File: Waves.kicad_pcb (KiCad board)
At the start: 2 copper layers, 49.8 x 106.5 mm, 147 parts, among them J1 AudioJack2_SwitchT, J10 AudioJack2_SwitchT, J11 Conn_01x04_Male, J12 Conn_01x04_Male, J13 AudioJack2_SwitchT, J14 AudioJack2_SwitchT, J15 Conn_02x05_Odd_Even, J2 AudioJack2_SwitchT, J3 AudioJack2_SwitchT, J4 AudioJack2_SwitchT, J5 AudioJack2_SwitchT, J6 AudioJack2_SwitchT, J7 AudioJack2_SwitchT, J8 AudioJack2_SwitchT, J9 AudioJack2_SwitchT, Q1 BC847, Q2 BC847, Q3 BC847, Q4 BC847, Q5 BC847, SW1 SW_Push, SW2 Rotary_Encoder_Switch, SW3 SW_Push_LED, SW4 SW_Push_LED, SW5 SW_Push_LED, U1 STM32G431, U2 AT25xxx, U3 IPS240x240, U4 PCM5100, U5 TL072, U6 LM1117-3.3, U7 LM1117-3.3, U8 MCP6004, U9 MCP6004, Y1 8MHz

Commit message: Placed front-side components.
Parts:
- C1, C10, C11, C12, C13, C14, C15, C16, C17, C18, C19, C2, C20, C21, C22, C23, C24, C25, C26, C27, C28, C29, C3, C30, C31, C32, C33, C34, C35, C36, C37, C38, C39, C4, C40, C41, C42, C43, C44, C45, C46, C47, C48, C49, C5, C50, C51, C52, C6, C7, C8, C9, D1, D2, D3, D4, FB1, FB2, FB3, J11, J12, J15, L1, Q1, Q2, Q3, Q4, Q5, R1, R10, R11, R12, R13, R14, R15, R16, R17, R18, R19, R2, R20, R21, R22, R23, R24, R25, R26, R27, R28, R29, R3, R30, R31, R32, R33, R34, R35, R36, R37, R38, R39, R4, R40, R41, R42, R43, R44, R45, R46, R5, R6, R7, R8, R9, TP1, TP2, TP3, TP4, TP5, TP6, U1, U2, U4, U5, U6, U7, U8, U9, Y1: moved to B.Cu
- moved R19 193.5 mm to (111.3, 147.6)
- moved Q3 192.8 mm to (107.1, 146.6)
- moved R20 191.7 mm to (111.3, 145.1)
- moved R21 165.0 mm to (142.9, 89.7), turned to 90 degrees
- moved Q4 162.4 mm to (146.4, 89.4), turned to 90 degrees
- moved SW4 157.9 mm to (144.6, 96.6)
- moved C25 147.6 mm to (181.0, 163.3)
- moved R6 147.6 mm to (185.0, 163.3)
- moved C21 147.3 mm to (176.8, 163.1)
- moved J9 146.7 mm to (109.1, 147.3)
- moved U5 146.1 mm to (162.3, 162.3)
- moved C20 145.2 mm to (170.7, 161.7)
- moved C22 144.0 mm to (185.0, 160.8)
- moved R10 144.0 mm to (181.0, 160.8)
- moved C28 143.4 mm to (176.6, 160.4)
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
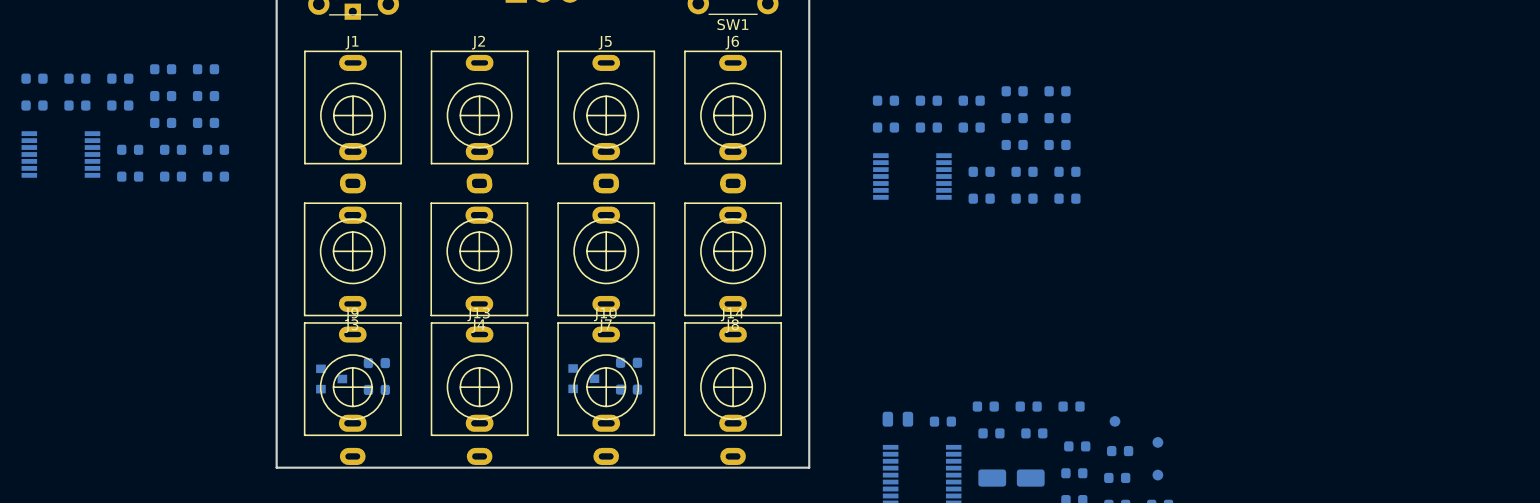
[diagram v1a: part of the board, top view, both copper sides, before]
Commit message: Corrected power supply for MCP6004.
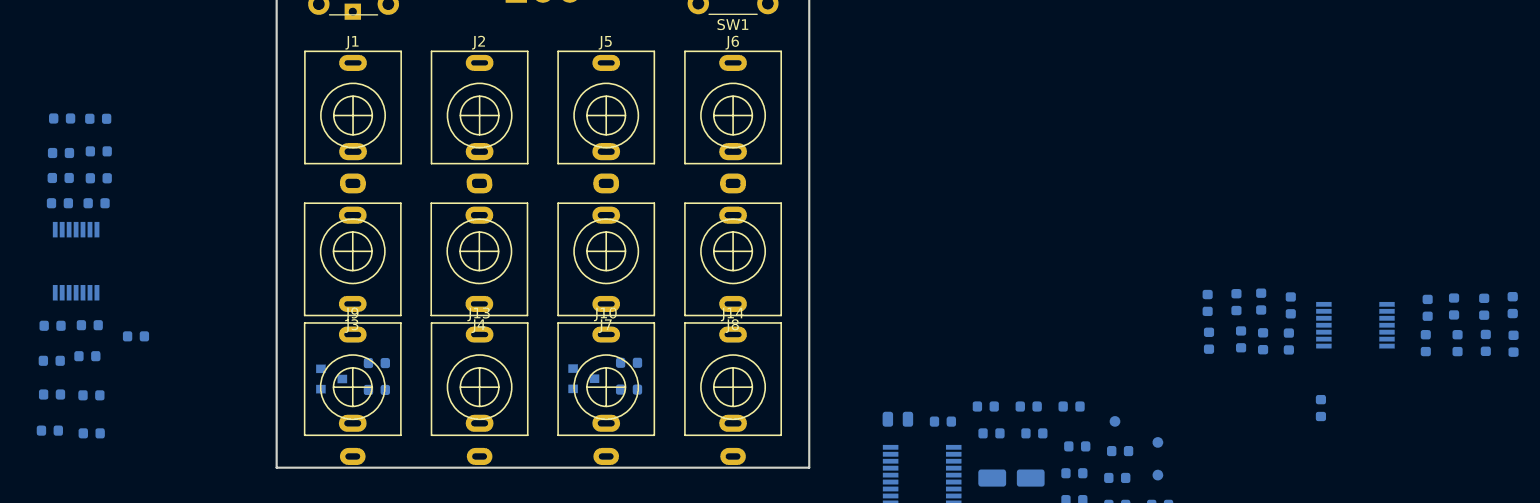
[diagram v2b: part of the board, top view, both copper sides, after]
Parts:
- removed C42, C48: 100n, Capacitor_SMD:C_0603_1608Metric
- moved R44 62.9 mm to (217.6, 143.3), turned to 270 degrees
- moved R43 55.8 mm to (215.0, 143.2), turned to 270 degrees
- moved R42 51.2 mm to (217.6, 139.6), turned to 90 degrees
- moved C52 45.4 mm to (212.4, 143.2), turned to 90 degrees
- moved R41 44.1 mm to (214.9, 139.8), turned to 90 degrees
- moved U9 43.7 mm to (202.8, 141.5)
- moved R45 42.9 mm to (209.6, 139.9), turned to 270 degrees
- moved R46 40.8 mm to (209.4, 143.2), turned to 90 degrees
- moved C47 39.4 mm to (199.6, 149.3), turned to 90 degrees
- moved R40 38.9 mm to (196.8, 139.7), turned to 270 degrees
- moved C51 38.3 mm to (212.1, 139.8), turned to 270 degrees
- moved R36 36.2 mm to (189.2, 143.0), turned to 270 degrees
- moved R39 35.8 mm to (196.6, 143.1), turned to 90 degrees
- moved R35 33.6 mm to (192.2, 142.8), turned to 270 degrees
- moved R24 31.1 mm to (84.7, 151.6)
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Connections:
- C41 pad 1: +12V -> +3.3VA
- C47 pad 1: +12V -> +3.3VA
- U8 pad 11: -12V -> GNDA
- U8 pad 4: +12V -> +3.3VA
- U9 pad 11: -12V -> GNDA
- U9 pad 4: +12V -> +3.3VA

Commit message: Re-annotated.
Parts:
- renumbered C43 to C42, C44 to C43, C45 to C44, C46 to C45, C47 to C46, C49 to C47, C50 to C48, C51 to C49, C52 to C50

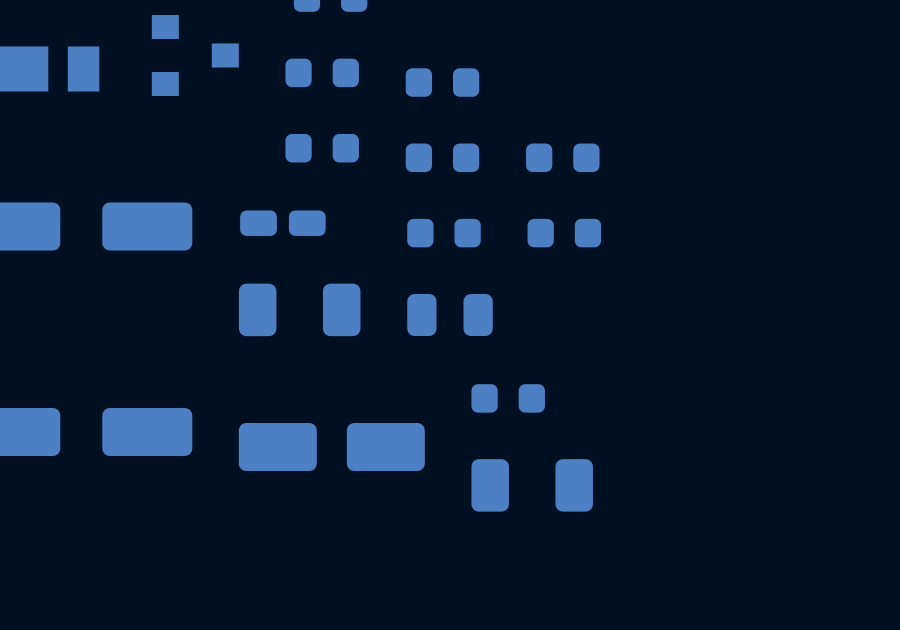
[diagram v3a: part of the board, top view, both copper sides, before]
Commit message: No split ground.
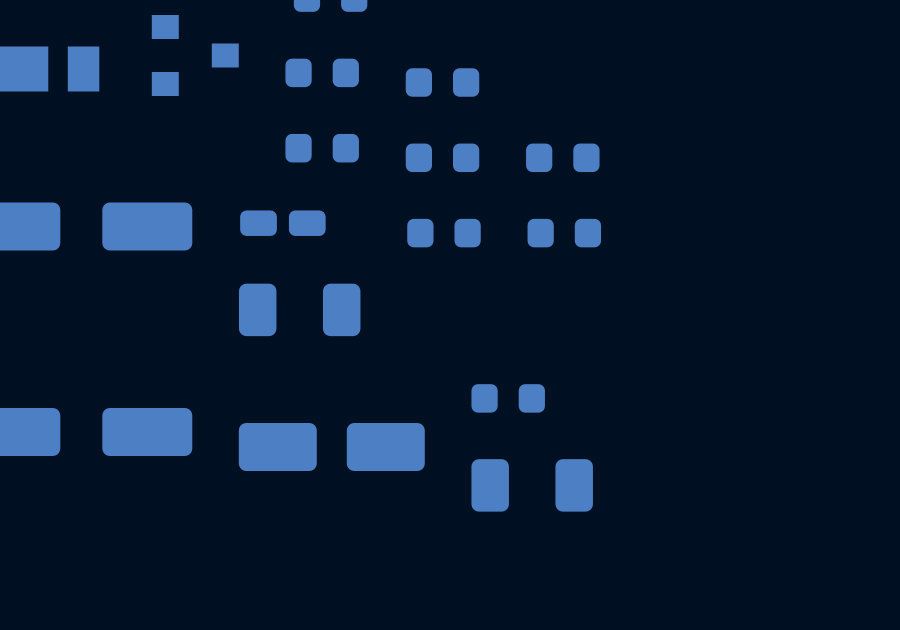
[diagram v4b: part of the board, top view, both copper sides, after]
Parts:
- removed R13: 0, Resistor_SMD:R_0805_2012Metric
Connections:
- C12 pad 2: GNDA -> GND
- C13 pad 2: GNDA -> GND
- C14 pad 2: GNDA -> GND
- C17 pad 2: GNDA -> GND
- C18 pad 2: GNDA -> GND
- C19 pad 2: GNDA -> GND
- C20 pad 2: GNDA -> GND
- C23 pad 2: GNDA -> GND
- C24 pad 2: GNDA -> GND
- C25 pad 2: GNDA -> GND
- C26 pad 1: GNDA -> GND
- C33 pad 2: GNDA -> GND
- C35 pad 2: GNDA -> GND
- C37 pad 2: GNDA -> GND
- C39 pad 2: GNDA -> GND
- C4 pad 2: GNDA -> GND
- C40 pad 2: GNDA -> GND
- C41 pad 2: GNDA -> GND
- C46 pad 2: GNDA -> GND
- C5 pad 2: GNDA -> GND
- D4 pad 1: GNDA -> GND
- U1 pad 19: GNDA -> GND
- U4 pad 3: GNDA -> GND
- U4 pad 9: GNDA -> GND
- U5 pad 3: GNDA -> GND
- U5 pad 5: GNDA -> GND
- U7 pad 1: GNDA -> GND
- U8 pad 10: GNDA -> GND
- U8 pad 11: GNDA -> GND
- U8 pad 12: GNDA -> GND
- U8 pad 3: GNDA -> GND
- U8 pad 5: GNDA -> GND
- U9 pad 10: GNDA -> GND
- U9 pad 11: GNDA -> GND
- U9 pad 12: GNDA -> GND
- U9 pad 3: GNDA -> GND
- U9 pad 5: GNDA -> GND

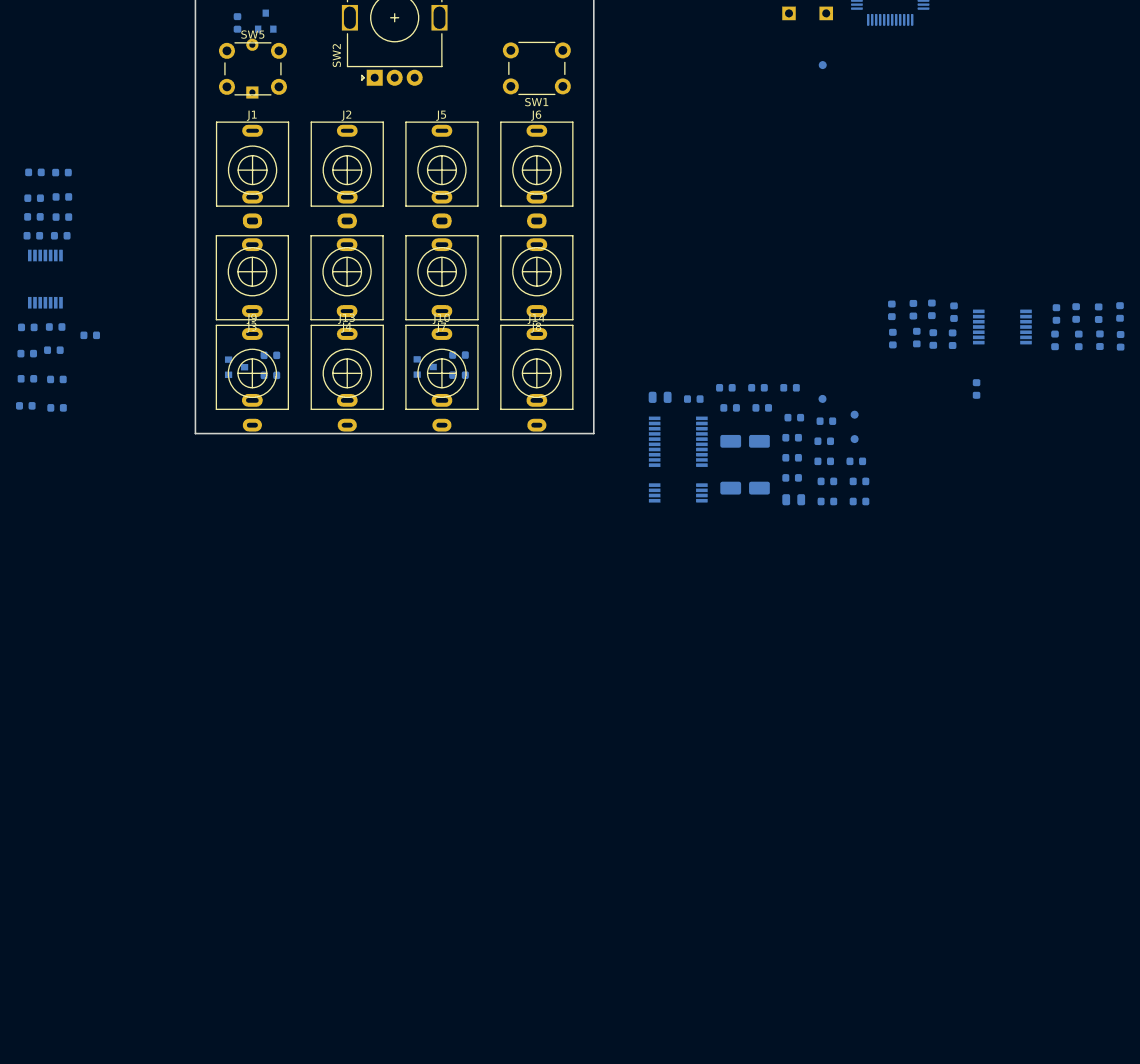
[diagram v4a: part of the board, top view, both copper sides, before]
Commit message: First pass of component placement.
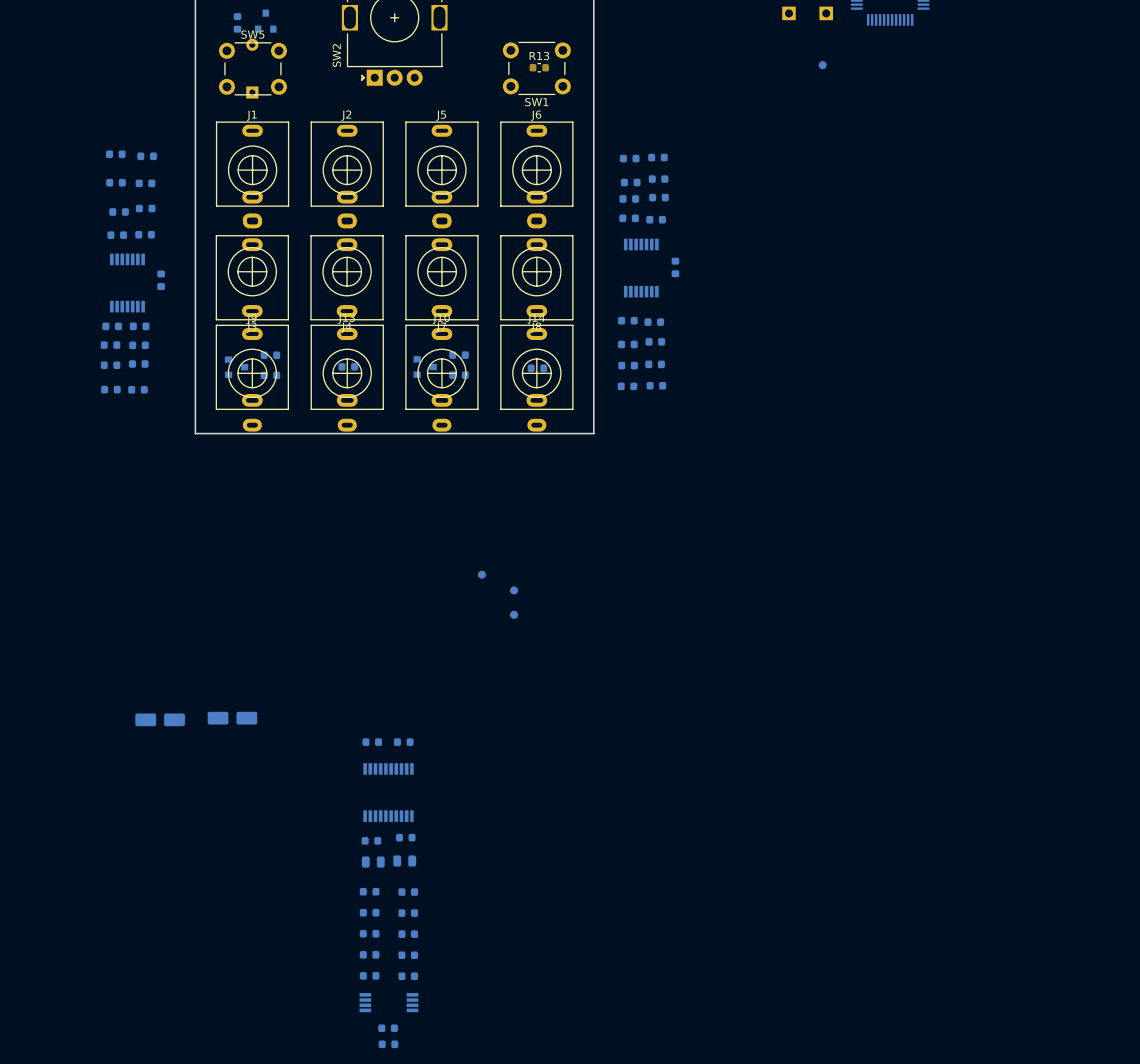
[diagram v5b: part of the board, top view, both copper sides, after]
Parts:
- added R13: 10k, Resistor_SMD:R_0603_1608Metric, F.Cu at (145.0, 109.1)
- moved C26 87.4 mm to (126.1, 229.2), turned to 180 degrees
- moved C25 87.3 mm to (126.1, 231.2), turned to 180 degrees
- moved R9 85.5 mm to (123.7, 222.6)
- moved C23 83.9 mm to (123.7, 214.7)
- moved R7 82.0 mm to (123.7, 217.4), turned to 180 degrees
- moved R6 81.9 mm to (128.6, 222.7), turned to 180 degrees
- moved R8 80.6 mm to (128.6, 217.4)
- moved C27 80.4 mm to (123.7, 220.0)
- moved R5 79.5 mm to (123.7, 212.1)
- moved C24 79.4 mm to (128.6, 220.1), turned to 180 degrees
- moved C20 78.6 mm to (97.6, 190.6)
- moved C17 77.0 mm to (124.0, 205.8), turned to 180 degrees
- moved C18 74.0 mm to (128.3, 205.4), turned to 180 degrees
- moved R10 73.4 mm to (128.6, 212.2), turned to 180 degrees
- moved U5 73.3 mm to (126.2, 226.0)
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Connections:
- C10 pad 1: RESET -> +3V3
- C11 pad 1: RESET -> +3V3
- C15 pad 1: RESET -> +3V3
- C16 pad 1: RESET -> +3V3
- C36 pad 1: RESET -> +3V3
- C38 pad 1: RESET -> +3V3
- C6 pad 1: RESET -> +3V3
- C7 pad 1: RESET -> +3V3
- C8 pad 1: RESET -> +3V3
- C9 pad 1: RESET -> +3V3
- J10 pad TN: RESET -> +3V3
- J9 pad TN: RESET -> +3V3
- R1 pad 1: RESET -> +3V3
- R17 pad 1: RESET -> +3V3
- R2 pad 1: RESET -> +3V3
- R20 pad 1: RESET -> +3V3
- U1 pad 1: RESET -> +3V3
- U1 pad 24: RESET -> +3V3
- U1 pad 36: RESET -> +3V3
- U1 pad 48: RESET -> +3V3
- U2 pad 3: RESET -> +3V3
- U2 pad 7: RESET -> +3V3
- U2 pad 8: RESET -> +3V3
- U3 pad 2: RESET -> +3V3
- U3 pad 7: RESET -> +3V3
- U4 pad 11: RESET -> +3V3
- U4 pad 17: RESET -> +3V3
- U4 pad 20: RESET -> +3V3
- U6 pad 2: RESET -> +3V3

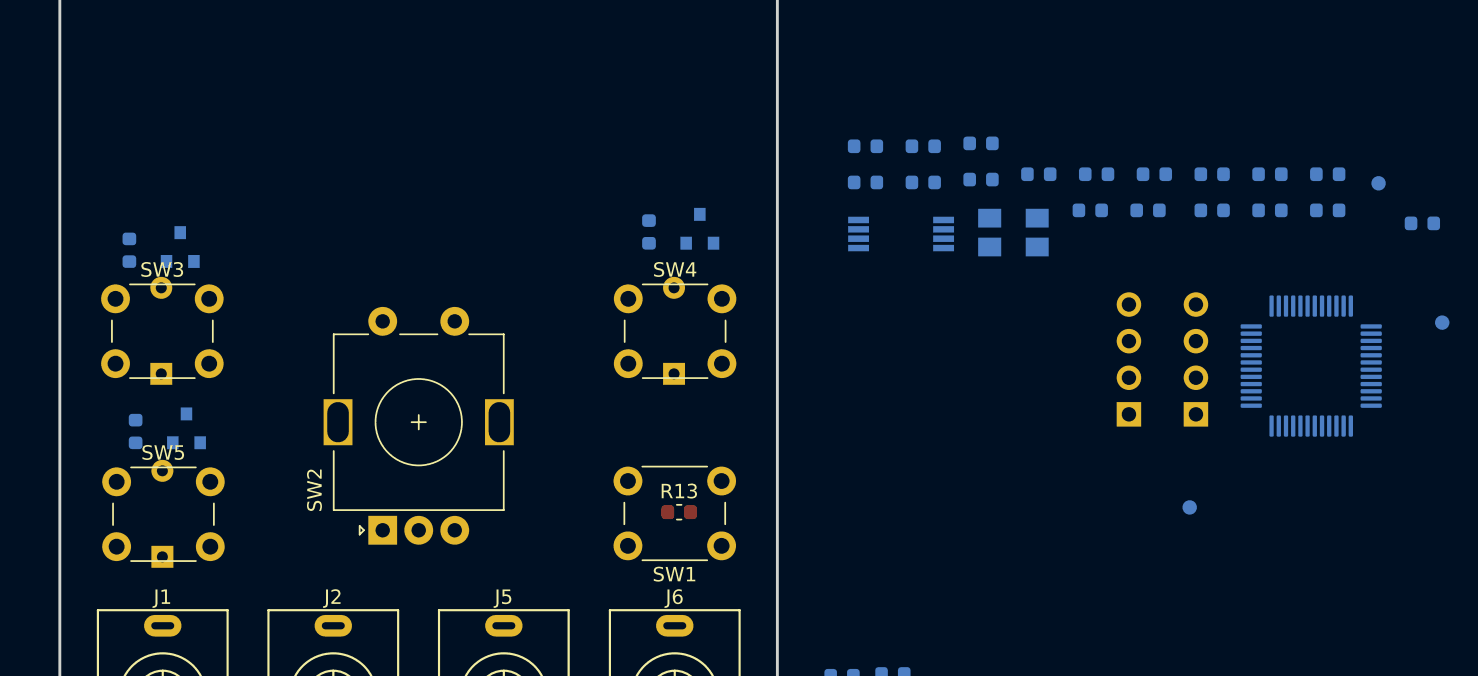
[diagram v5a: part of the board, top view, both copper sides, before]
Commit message: Added fourth led-button and movde reset switch.
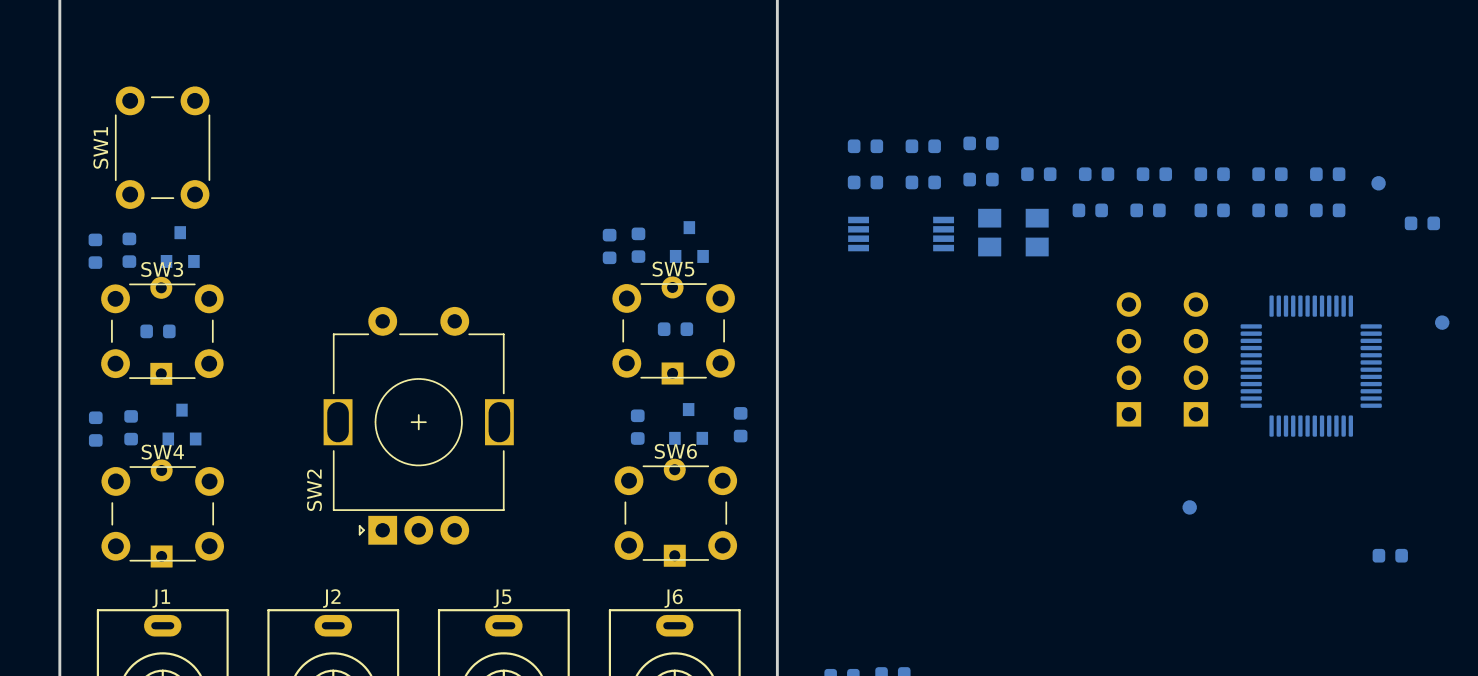
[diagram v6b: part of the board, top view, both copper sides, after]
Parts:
- removed the R21 at (142.9, 89.7)
- added C1: 100n, Capacitor_SMD:C_0603_1608Metric, B.Cu at (108.8, 96.6)
- added C5: 100n, Capacitor_SMD:C_0603_1608Metric, B.Cu at (144.7, 96.4)
- added Q6: BC847, Package_TO_SOT_SMD:SOT-23, B.Cu at (145.6, 103.0)
- added R1: 4k7, Resistor_SMD:R_0603_1608Metric, B.Cu at (104.4, 91.0)
- added R2: 4k7, Resistor_SMD:R_0603_1608Metric, B.Cu at (104.5, 103.4)
- added R25: 47, Resistor_SMD:R_0603_1608Metric, B.Cu at (106.9, 103.3)
- added R51: 47, Resistor_SMD:R_0603_1608Metric, B.Cu at (142.1, 103.2)
- added R7: 4k7, Resistor_SMD:R_0603_1608Metric, B.Cu at (149.2, 103.0)
- added R8: 4k7, Resistor_SMD:R_0603_1608Metric, B.Cu at (140.1, 90.7)
- added SW6: SW_Push_LED, Local:SW_PUSH_LED_6mm, F.Cu at (144.7, 109.2)
- R5: renamed from R13; moved to B.Cu
- moved R5 49.4 mm to (194.3, 112.1)
- moved SW1 47.7 mm to (106.9, 87.1), turned to 90 degrees
- moved Q4 38.4 mm to (110.5, 103.0)
- moved SW4 37.8 mm to (109.0, 109.3)
- moved SW5 37.6 mm to (144.5, 96.6)
- moved Q5 37.2 mm to (145.7, 90.4)
- moved R26 37.2 mm to (142.1, 90.6)
- renumbered C8 to C10, C9 to C11, C10 to C12, C11 to C13, C12 to C14, C13 to C15, C14 to C16, C15 to C17, C16 to C18, C17 to C19, C1 to C2, C18 to C20, C19 to C21, C20 to C22, C21 to C23, C22 to C24, C23 to C25, C24 to C26, C25 to C27, C26 to C28, C27 to C29, C2 to C3, C28 to C30, C29 to C31, C30 to C32, C31 to C33, C32 to C34, C33 to C35, C34 to C36, C35 to C37, C36 to C38, C37 to C39, C3 to C4, C38 to C40, C39 to C41, C40 to C42, C41 to C43, C42 to C44, C43 to C45, C44 to C46, C45 to C47, C46 to C48, C47 to C49, C48 to C50, C49 to C51, C50 to C52, C4 to C6, C5 to C7, C6 to C8, C7 to C9, R5 to R10, R6 to R11, R7 to R12, R8 to R13, R9 to R14, R10 to R15, R11 to R16, R12 to R17, R14 to R18, R15 to R19, R16 to R20, R17 to R21, R18 to R22, R19 to R23, R20 to R24, R22 to R26, R23 to R27, R24 to R28, R25 to R29, R1 to R3, R26 to R30, R27 to R31, R28 to R32, R29 to R33, R30 to R34, R31 to R35, R32 to R36, R33 to R37, R34 to R38, R35 to R39, R2 to R4, R36 to R40, R37 to R41, R38 to R42, R39 to R43, R40 to R44, R41 to R45, R42 to R46, R43 to R47, R44 to R48, R45 to R49, R46 to R50, R3 to R6, R4 to R9
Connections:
- U1 pad 12: BTN2 -> BTN1
- U1 pad 3: BTN1 -> LED2
- U1 pad 34: LED3 -> LED4
- U1 pad 4: LED2 -> LED3
